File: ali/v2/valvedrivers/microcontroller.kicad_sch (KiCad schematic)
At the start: 48 parts, among them J1 Conn_02x01, J2 Conn_01x05, J3 USB_C_Receptacle_USB2.0_16P, J4 Screw_Terminal_01x02, J5 Screw_Terminal_01x02, J6 Screw_Terminal_01x02, SW1 SKRPANE010, U1 STM32H563RIV6, U2 LTV-816S, U3 AP2112K-3.3, Y1 25 MHz

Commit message: Idk why this package change keeps happening
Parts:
- U1: footprint Package_DFN_QFN:QFN-68-1EP_8x8mm_P0.4mm_EP6.4x6.4mm -> APRL_Package_QFN:QFN-68-1EP_8x8mm_P0.4mm_EP6.4x6.4mm

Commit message: Globally remove LCSC labels, update MPNs and IOCs, add +5V monitoring to DAQs, fix some footprints
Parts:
- F2: MPN FLR_178.6165 -> 178.6165.0001
- R10, R5, R6, R7, R8, R9: MPN RC0603FR-0710KL -> RC0603FR-0710KL
- U2: footprint APRL_Package:4-SMD -> Package_DIP:DIP-4_W7.62mm

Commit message: Fix  models for kicad 10.0.5
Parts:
- U2: footprint Package_DIP:DIP-4_W7.62mm -> APRL_Package:4-SMD

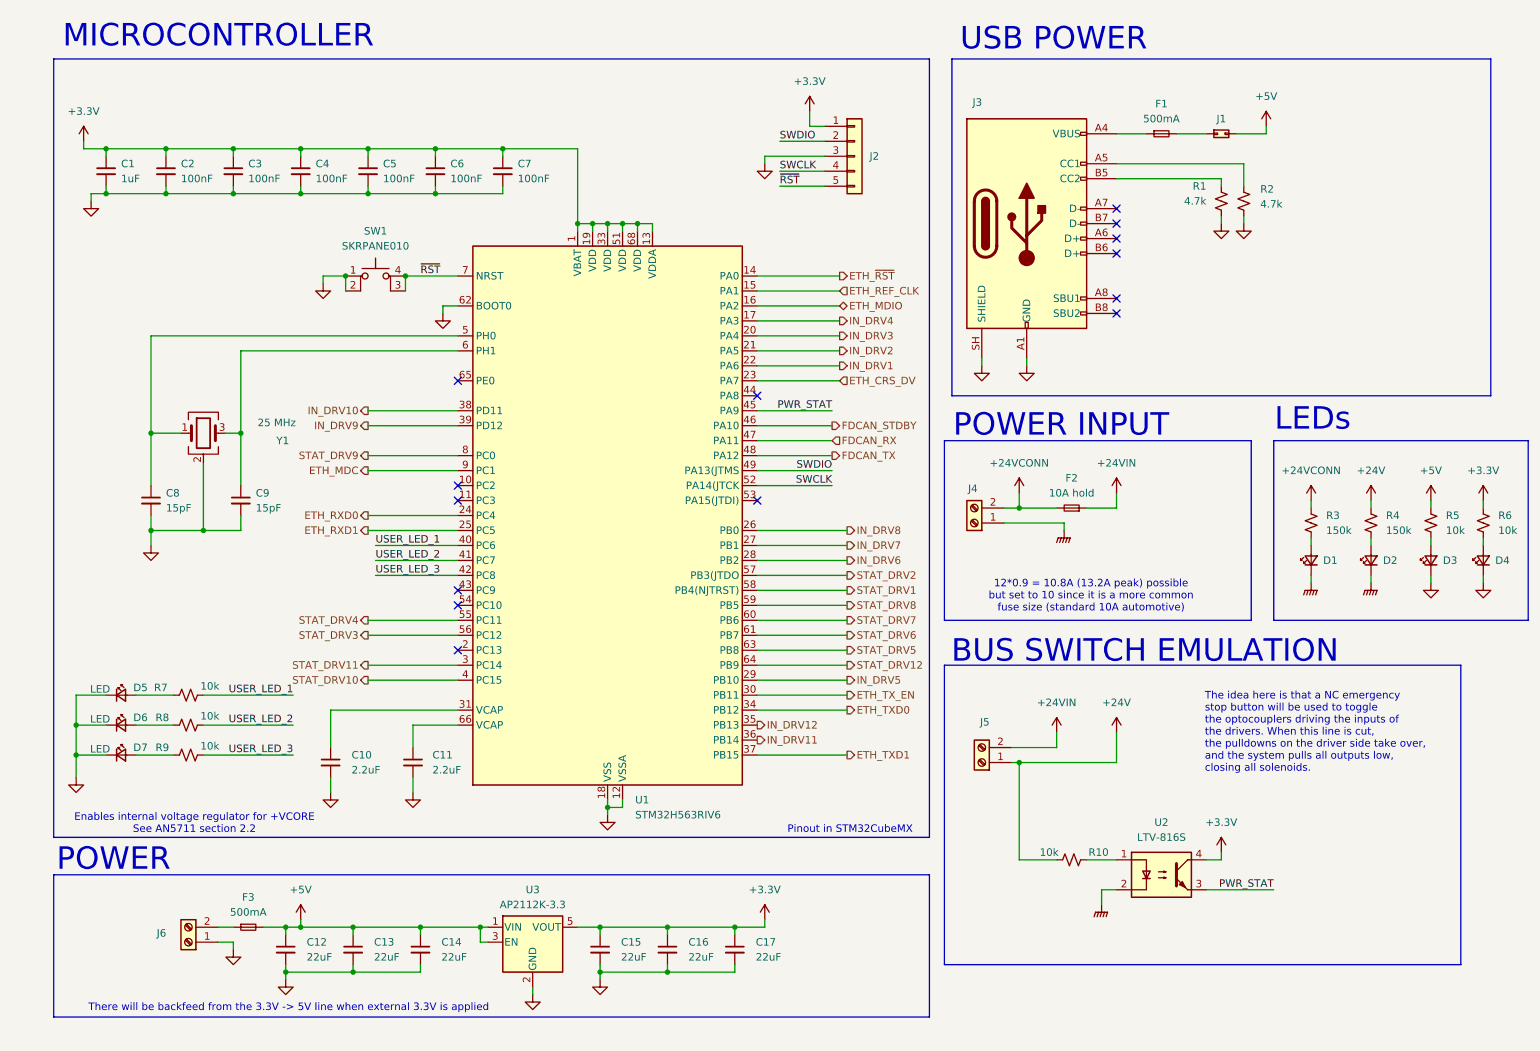
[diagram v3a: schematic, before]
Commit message: the great flatpak and kicad 10.0.6 migration
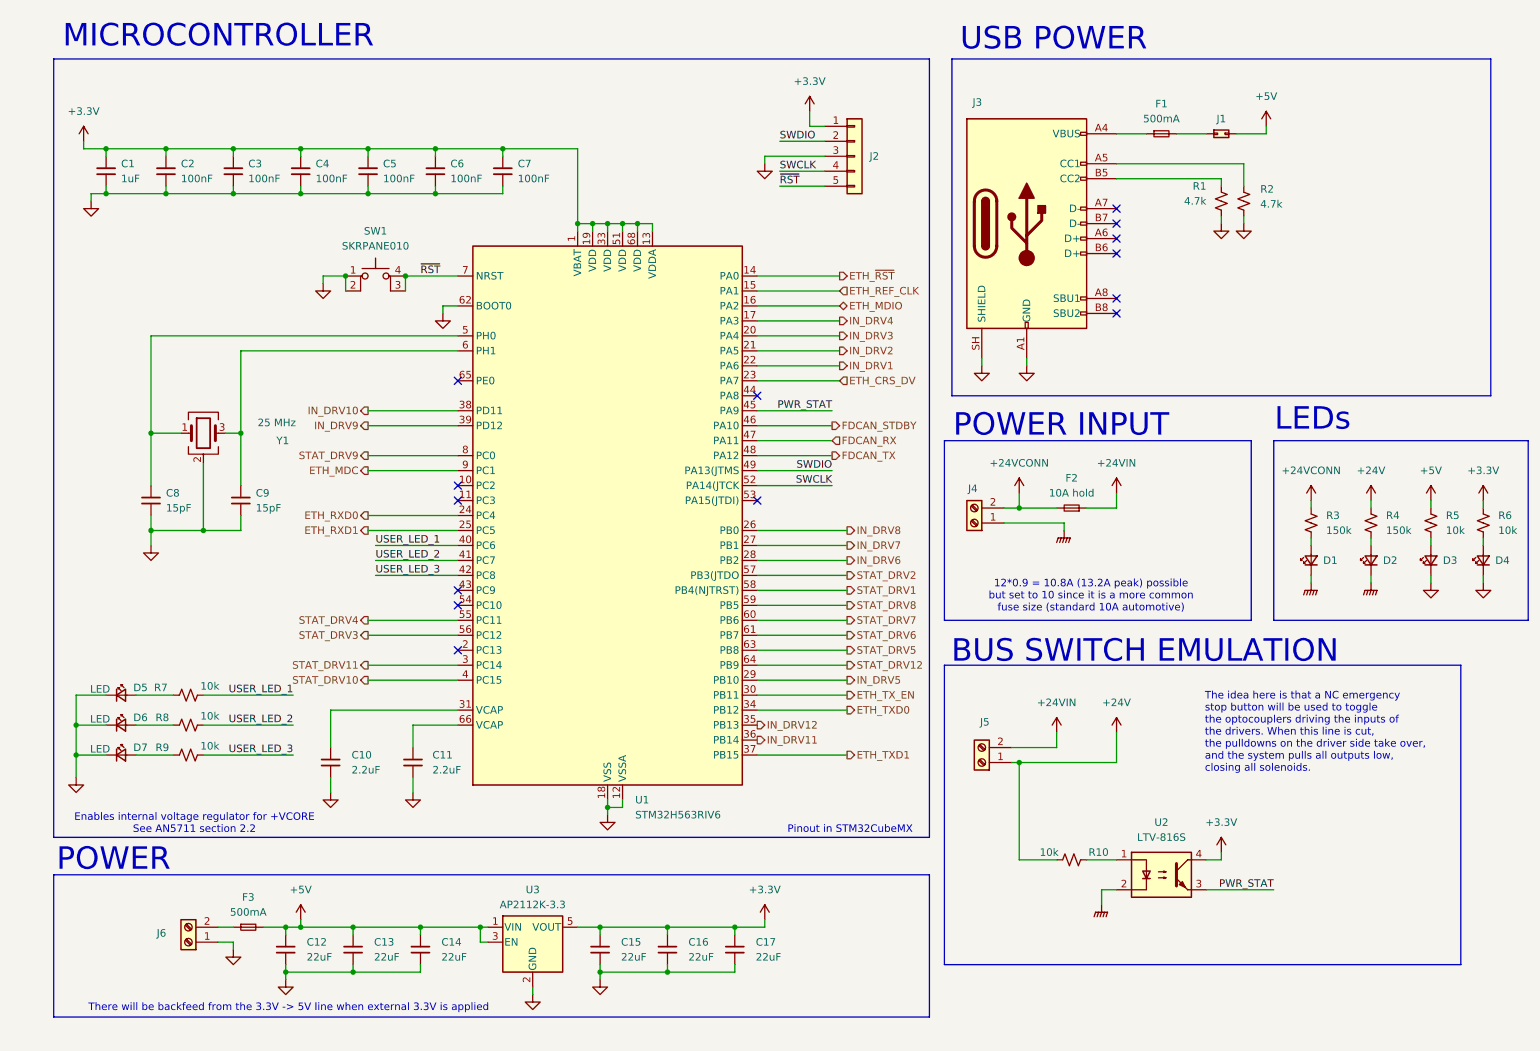
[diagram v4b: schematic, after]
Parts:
- U1: footprint APRL_Package_QFN:QFN-68-1EP_8x8mm_P0.4mm_EP6.4x6.4mm -> Package_DFN_QFN:QFN-68-1EP_8x8mm_P0.4mm_EP6.4x6.4mm
- U2: footprint APRL_Package:4-SMD -> Package_DIP:DIP-4_W7.62mm

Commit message: The other half of the great 10.0.6 migration
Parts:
- U1: footprint Package_DFN_QFN:QFN-68-1EP_8x8mm_P0.4mm_EP6.4x6.4mm -> APRL_Package_QFN:QFN-68-1EP_8x8mm_P0.4mm_EP6.4x6.4mm; symbol MCU_ST_STM32H5:STM32H563RIVx -> APRL_MCU:STM32H563RIVx

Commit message: Add ignition port to valve driver board, set up CANBUS keepouts
Daniel please don't see this I am embarassed
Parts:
- added J7: Conn_01x05, APRL_Connector_Molex:Molex_CLIK-Mate_503159-0501_1x05-1MP_P1.50mm_Vertical, symbol Connector_Generic:Conn_01x05
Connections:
- net +3.3V: now also J7.5 (Pin_5)
- net +5V: now also J7.1 (Pin_1)
- net GND: now also J7.2 (Pin_2)
- net IGNIG: now reaches U1.43 (PC9)
- net IGNIG: now also J7.4 (Pin_4)
- net IGNIG_STAT: now reaches U1.44 (PA8)
- net IGNIG_STAT: now also J7.3 (Pin_3)
- no-connect marks 14 -> 12
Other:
- note added: "IGNIG"
- note added: "Maybe consider adding a zener here to set a +24V UV threshold alert?"
- moved on the sheet: C12, C13, C14, C15, C16, C17, F3, J6, U3

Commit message: Fix 50R/60R widths
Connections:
- net IGNIG_STAT renamed BRK_WIRE
- net PWR_STAT renamed +24V_STAT

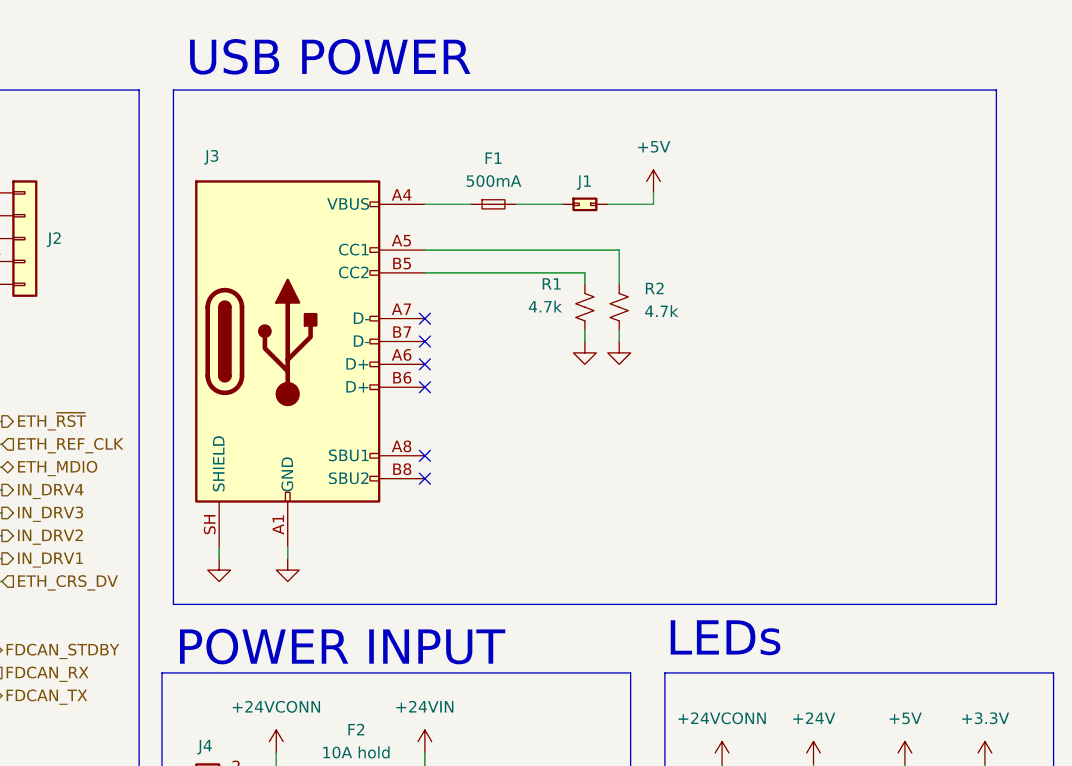
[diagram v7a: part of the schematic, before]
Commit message: Document setup, update template, and use an ampersand when referring to APRL
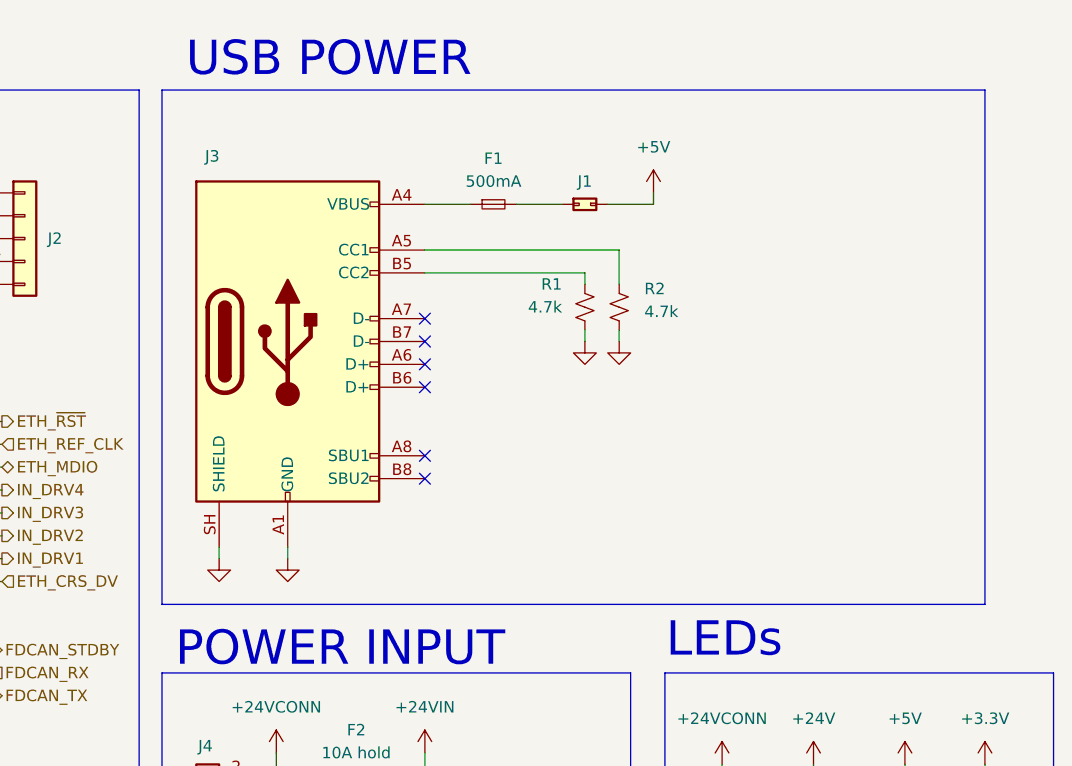
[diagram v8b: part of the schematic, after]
